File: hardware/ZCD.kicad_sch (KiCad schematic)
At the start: 4 parts

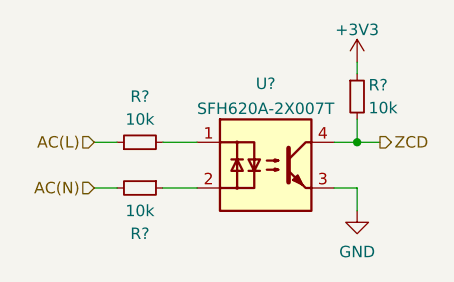
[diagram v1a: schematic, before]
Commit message: assigned footprints
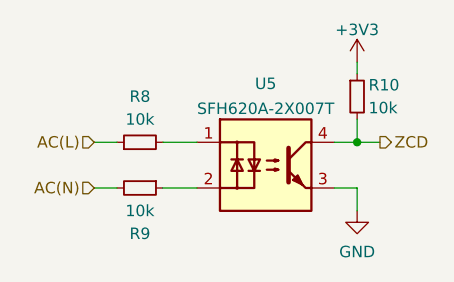
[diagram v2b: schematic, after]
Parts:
- R10: renamed from R?; footprint (none) -> Resistor_SMD:R_0603_1608Metric
- R8, R9: renamed from R?; footprint (none) -> Resistor_SMD:R_1206_3216Metric
- gave numbers to parts that had none: 1
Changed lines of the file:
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@@
   (symbol (lib_id "Device:R_Small") (at 138.43 105.41 270) (unit 1)
     (in_bom yes) (on_board yes)
-    (property "Reference" "R?" (id 0) (at 138.43 110.49 90))
+    (property "Reference" "R9" (id 0) (at 138.43 110.49 90))
     (property "Value" "10k" (id 1) (at 138.43 107.95 90))
-    (property "Footprint" "" (id 2) (at 138.43 105.41 0)
+    (property "Footprint" "Resistor_SMD:R_1206_3216Metric" (id 2) (at 138.43 105.41 0)
       (effects (font (size 1.27 1.27)) hide)
     )
@@
   (symbol (lib_id "Device:R_Small") (at 162.56 95.25 0) (unit 1)
     (in_bom yes) (on_board yes)
-    (property "Reference" "R?" (id 0) (at 163.83 93.98 0)
+    (property "Reference" "R10" (id 0) (at 163.83 93.98 0)
       (effects (font (size 1.27 1.27)) (justify left))
     )
@@
       (effects (font (size 1.27 1.27)) (justify left))
     )
-    (property "Footprint" "" (id 2) (at 162.56 95.25 0)
+    (property "Footprint" "Resistor_SMD:R_0603_1608Metric" (id 2) (at 162.56 95.25 0)
       (effects (font (size 1.27 1.27)) hide)
     )
@@
   (symbol (lib_id "power:+3V3") (at 162.56 91.44 0) (unit 1)
     (in_bom yes) (on_board yes) (fields_autoplaced)
-    (property "Reference" "#PWR?" (id 0) (at 162.56 95.25 0)
+    (property "Reference" "#PWR033" (id 0) (at 162.56 95.25 0)
       (effects (font (size 1.27 1.27)) hide)
     )
@@
   (symbol (lib_id "power:GND") (at 162.56 107.95 0) (unit 1)
     (in_bom yes) (on_board yes) (fields_autoplaced)
-    (property "Reference" "#PWR?" (id 0) (at 162.56 114.3 0)
+    (property "Reference" "#PWR034" (id 0) (at 162.56 114.3 0)
       (effects (font (size 1.27 1.27)) hide)
     )
@@
   (symbol (lib_id "Device:R_Small") (at 138.43 100.33 90) (unit 1)
     (in_bom yes) (on_board yes)
-    (property "Reference" "R?" (id 0) (at 138.43 95.25 90))
+    (property "Reference" "R8" (id 0) (at 138.43 95.25 90))
     (property "Value" "10k" (id 1) (at 138.43 97.79 90))
-    (property "Footprint" "" (id 2) (at 138.43 100.33 0)
+    (property "Footprint" "Resistor_SMD:R_1206_3216Metric" (id 2) (at 138.43 100.33 0)
       (effects (font (size 1.27 1.27)) hide)
     )
@@
   (symbol (lib_id "Isolator:SFH620A-2X007T") (at 152.4 102.87 0) (unit 1)
     (in_bom yes) (on_board yes) (fields_autoplaced)
-    (property "Reference" "U?" (id 0) (at 152.4 93.8235 0))
+    (property "Reference" "U5" (id 0) (at 152.4 93.8235 0))
     (property "Value" "SFH620A-2X007T" (id 1) (at 152.4 96.5986 0))
     (property "Footprint" "Package_DIP:SMDIP-4_W9.53mm_Clearance8mm" (id 2) (at 152.4 113.03 0)

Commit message: finished layout
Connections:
- net AC(L) renamed AC1
- net AC(N) renamed AC2
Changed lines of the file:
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@@
     (stroke (width 0) (type default) (color 0 0 0 0))
   )
-  (hierarchical_label "AC(N)" (shape input) (at 133.35 105.41 180)
+  (hierarchical_label "AC1" (shape input) (at 133.35 100.33 180)
     (effects (font (size 1.27 1.27)) (justify right))
   )
@@
     (effects (font (size 1.27 1.27)) (justify left))
   )
-  (hierarchical_label "AC(L)" (shape input) (at 133.35 100.33 180)
+  (hierarchical_label "AC2" (shape input) (at 133.35 105.41 180)
     (effects (font (size 1.27 1.27)) (justify right))
   )
